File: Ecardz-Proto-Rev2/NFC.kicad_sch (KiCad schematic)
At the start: 30 parts, among them IC1 M24LR04E-RMN6T/2, J5 Conn_01x02

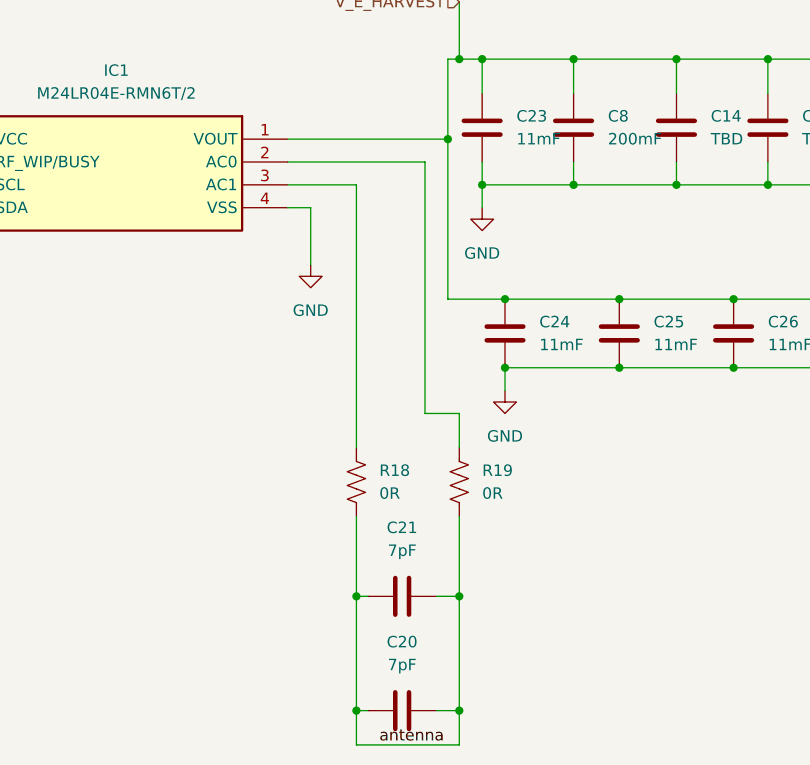
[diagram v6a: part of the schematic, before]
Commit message: final fit check complete.
added updated step, wrl, gerbers and svg file used for silkscreen
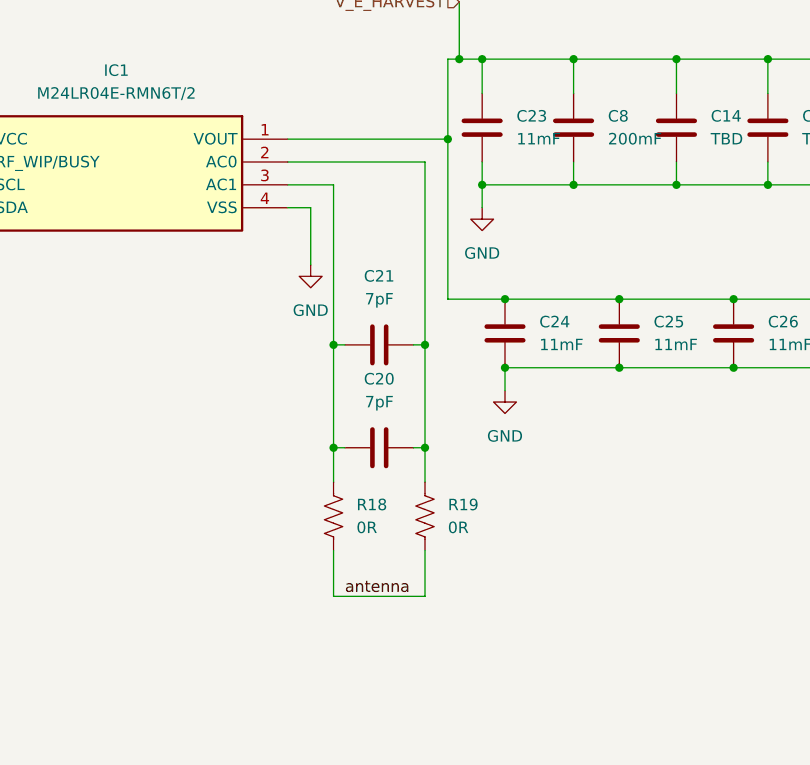
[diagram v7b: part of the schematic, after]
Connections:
- net antenna: no longer C20.1, C20.2, C21.1, C21.2
- net at IC1.3 (AC1), R18.2: now also C20.1, C21.1
- net at IC1.2 (AC0), R19.2: now also C20.2, C21.2
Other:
- moved on the sheet: R18, R19
